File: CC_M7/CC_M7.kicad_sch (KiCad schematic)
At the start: 0 parts

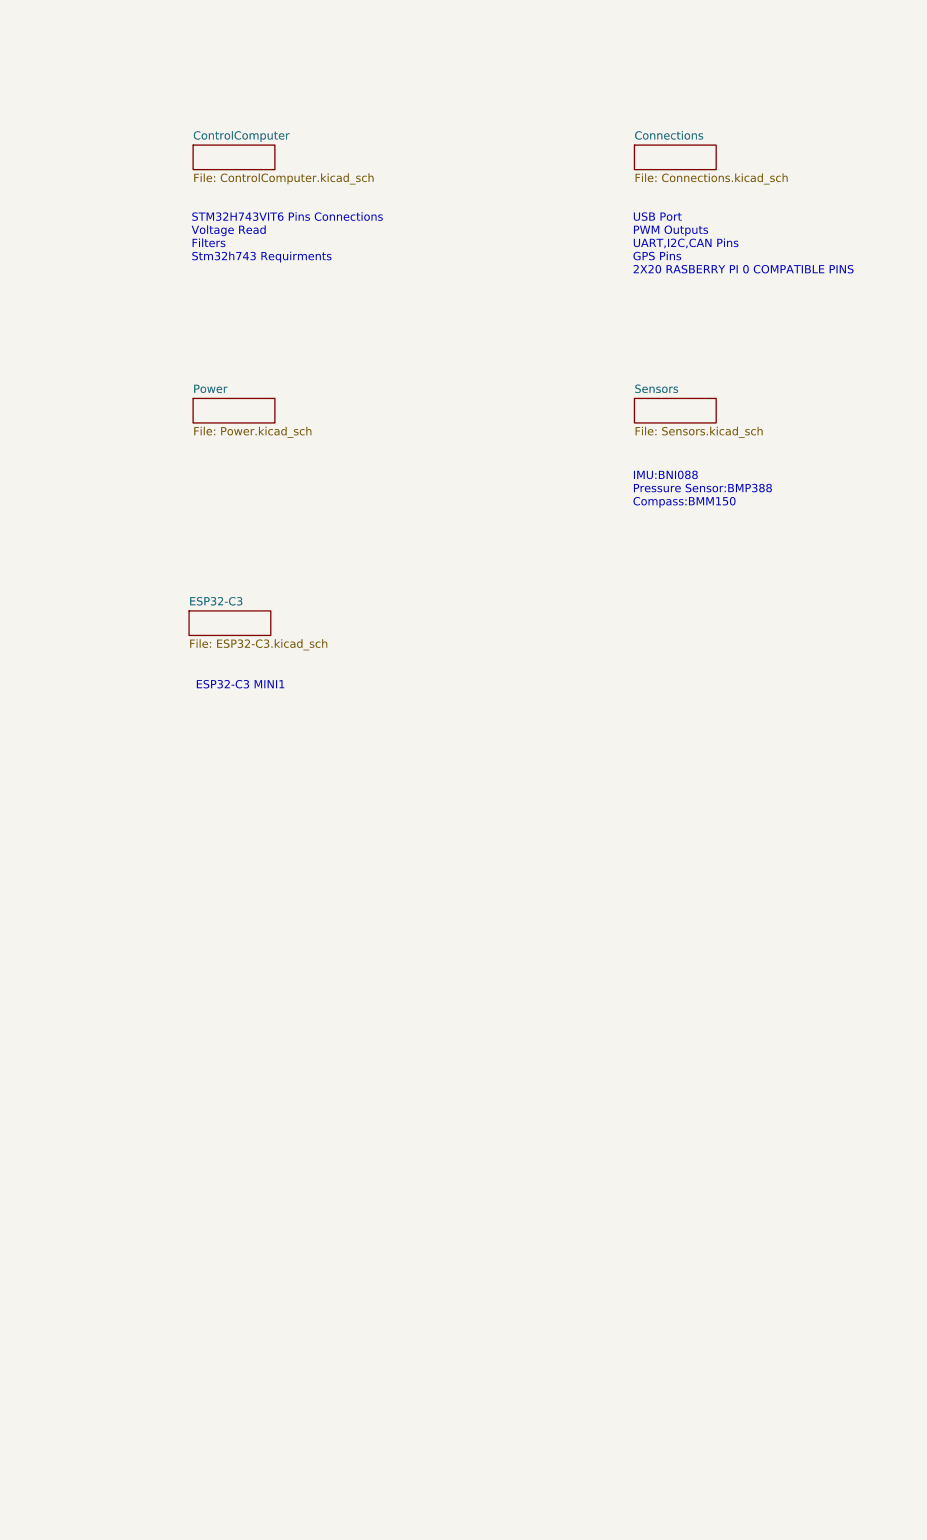
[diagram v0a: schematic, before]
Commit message: update schematic
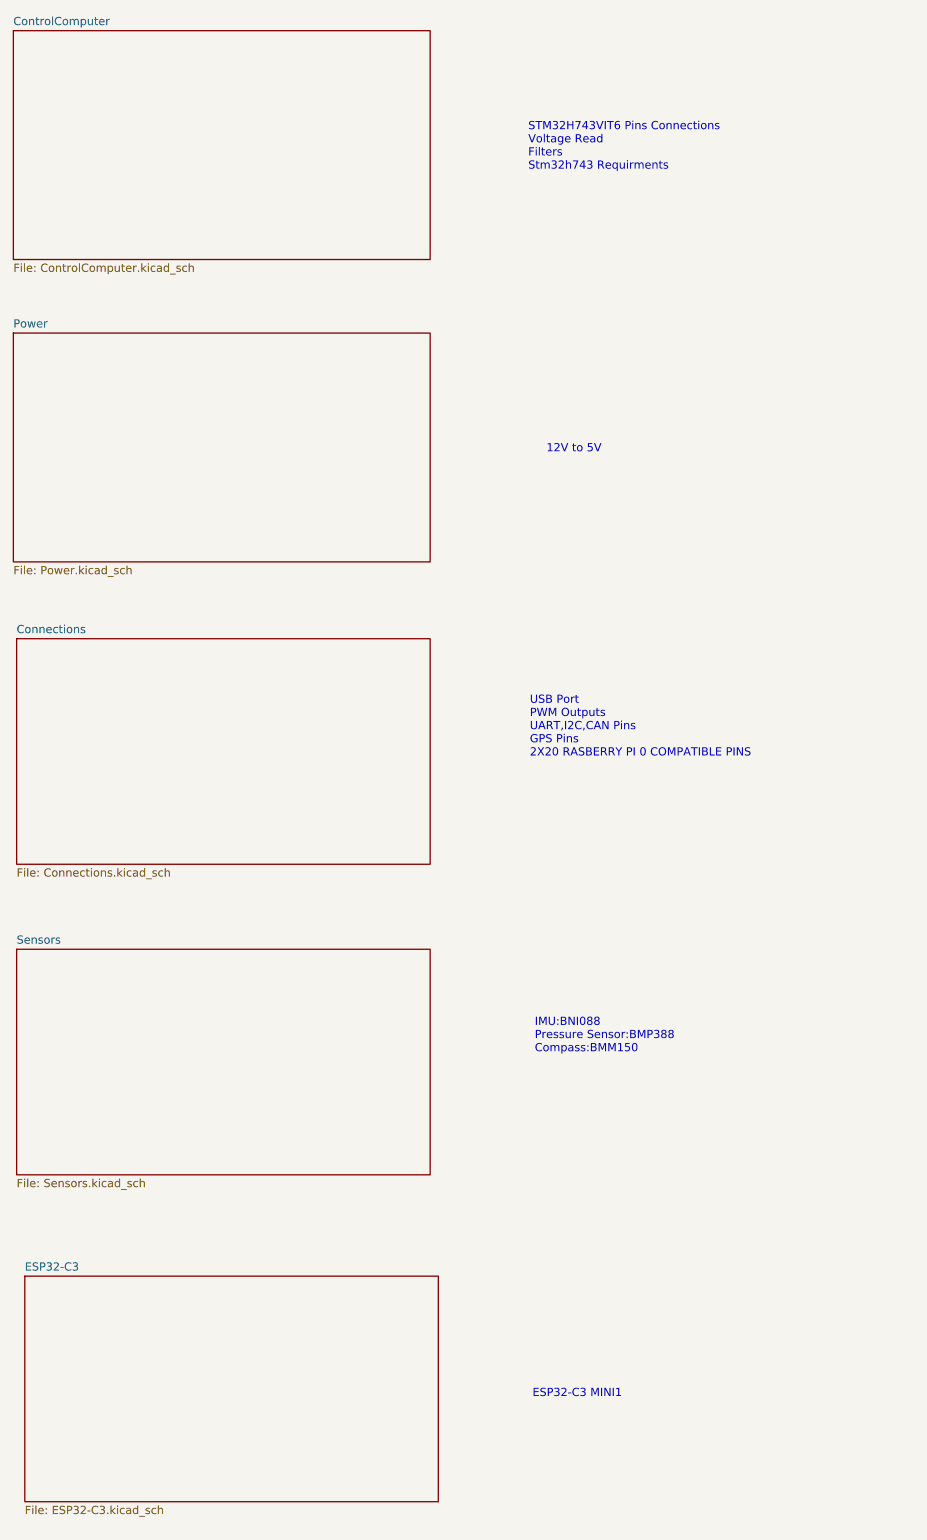
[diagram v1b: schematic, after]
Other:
- note added: "12V to 5V"
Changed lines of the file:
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@@
 		(comment 1 "Stm32 F7 Control Cart")
 	)
+	(text "12V to 5V"
+		(exclude_from_sim no)
+		(at 116.332 85.344 0)
+		(effects
+			(font
+				(size 1.27 1.27)
+			)
+		)
+	)
 	(text "USB Port\nPWM Outputs\nUART,I2C,CAN Pins\nGPS Pins\n2X20 RASBERRY PI 0 COMPATIBLE PINS"
 		(exclude_from_sim no)
-		(at 125.476 53.594 0)
+		(at 109.474 128.524 0)
 		(effects
 			(font
@@
 	(text "ESP32-C3 MINI1"
 		(exclude_from_sim no)
-		(at 64.516 122.174 0)
+		(at 116.84 232.156 0)
 		(effects
 			(font
@@
 	(text "STM32H743VIT6 Pins Connections\nVoltage Read\nFilters\nStm32h743 Requirments"
 		(exclude_from_sim no)
-		(at 56.896 52.578 0)
+		(at 109.22 38.354 0)
 		(effects
 			(font
@@
 	(text "IMU:BNI088\nPressure Sensor:BMP388\nCompass:BMM150\n"
 		(exclude_from_sim no)
-		(at 125.476 91.694 0)
+		(at 110.236 176.53 0)
 		(effects
 			(font
@@
 	)
 	(sheet
-		(at 57.15 38.1)
-		(size 12.7 3.81)
+		(at 29.21 20.32)
+		(size 64.77 35.56)
 		(fields_autoplaced yes)
 		(stroke
@@
 		)
 		(property "Sheetname" "ControlComputer"
-			(at 57.15 37.3884 0)
+			(at 29.21 19.6084 0)
 			(effects
 				(font
@@
 		)
 		(property "Sheetfile" "ControlComputer.kicad_sch"
-			(at 57.15 42.4946 0)
+			(at 29.21 56.4646 0)
 			(effects
 				(font
@@
 	)
 	(sheet
-		(at 56.515 110.49)
-		(size 12.7 3.81)
+		(at 30.988 213.868)
+		(size 64.262 35.052)
 		(fields_autoplaced yes)
 		(stroke
@@
 		)
 		(property "Sheetname" "ESP32-C3"
-			(at 56.515 109.7784 0)
+			(at 30.988 213.1564 0)
 			(effects
 				(font
@@
 		)
 		(property "Sheetfile" "ESP32-C3.kicad_sch"
-			(at 56.515 114.8846 0)
+			(at 30.988 249.5046 0)
 			(effects
 				(font
@@
 	)
 	(sheet
-		(at 125.73 38.1)
-		(size 12.7 3.81)
+		(at 29.718 114.808)
+		(size 64.262 35.052)
 		(fields_autoplaced yes)
 		(stroke
@@
 		)
 		(property "Sheetname" "Connections"
-			(at 125.73 37.3884 0)
+			(at 29.718 114.0964 0)
 			(effects
 				(font
@@
 		)
 		(property "Sheetfile" "Connections.kicad_sch"
-			(at 125.73 42.4946 0)
+			(at 29.718 150.4446 0)
 			(effects
 				(font
@@
 	)
 	(sheet
-		(at 125.73 77.47)
-		(size 12.7 3.81)
+		(at 29.718 163.068)
+		(size 64.262 35.052)
 		(fields_autoplaced yes)
 		(stroke
@@
 		)
 		(property "Sheetname" "Sensors"
-			(at 125.73 76.7584 0)
+			(at 29.718 162.3564 0)
 			(effects
 				(font
@@
 		)
 		(property "Sheetfile" "Sensors.kicad_sch"
-			(at 125.73 81.8646 0)
+			(at 29.718 198.7046 0)
 			(effects
 				(font
@@
 	)
 	(sheet
-		(at 57.15 77.47)
-		(size 12.7 3.81)
+		(at 29.21 67.31)
+		(size 64.77 35.56)
 		(fields_autoplaced yes)
 		(stroke
@@
 		)
 		(property "Sheetname" "Power"
-			(at 57.15 76.7584 0)
+			(at 29.21 66.5984 0)
 			(effects
 				(font
@@
 		)
 		(property "Sheetfile" "Power.kicad_sch"
-			(at 57.15 81.8646 0)
-			(effects
-				(font
+			(at 29.21 103.4546 0)
+			(effects
+				(font

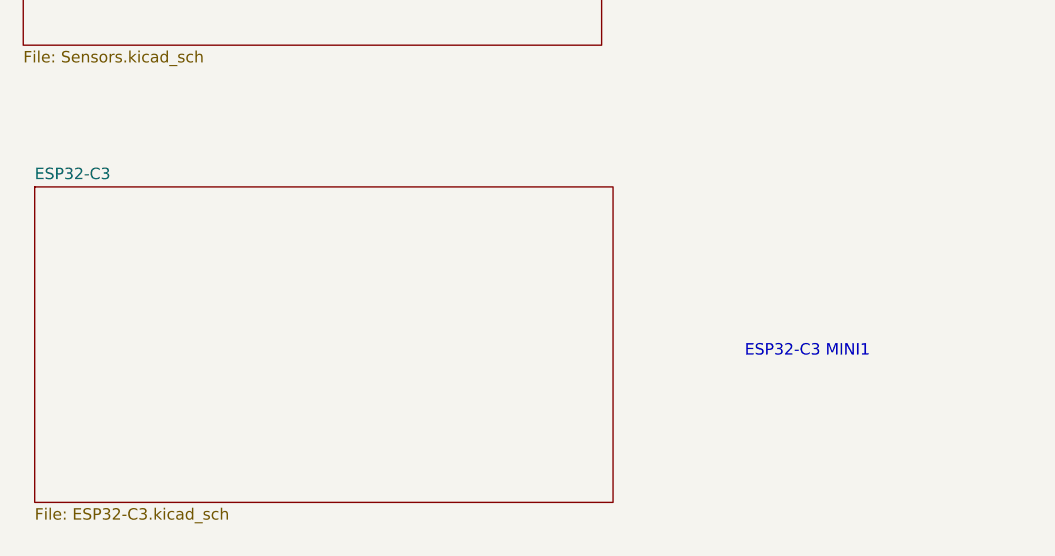
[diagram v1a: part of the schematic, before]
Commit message: nRF52820+nRf21540 add
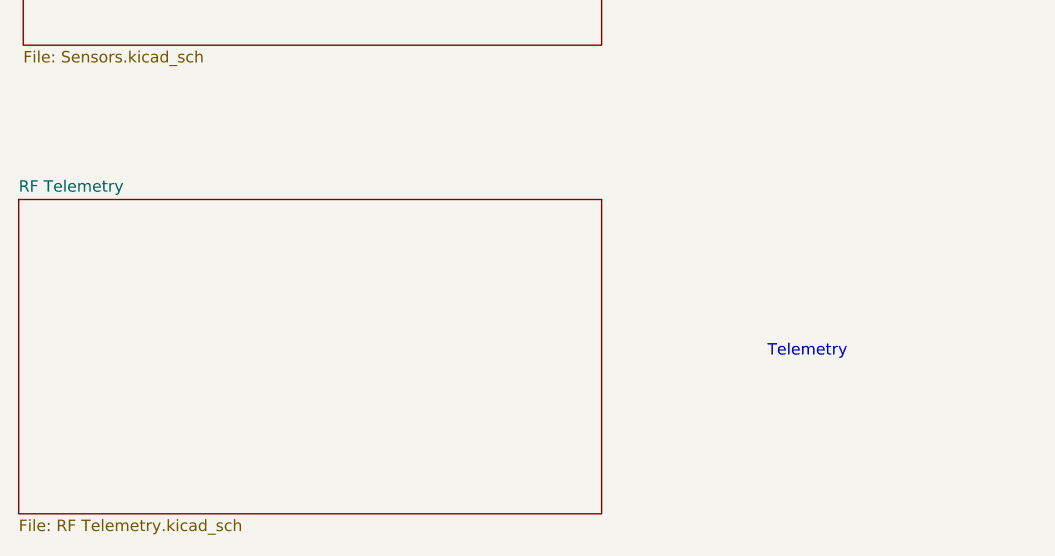
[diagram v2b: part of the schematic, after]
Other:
- removed sheet ESP32-C3
- added sheet RF Telemetry (RF Telemetry.kicad_sch)
- note added: "Telemetry"
- note removed: "ESP32-C3 MINI1"
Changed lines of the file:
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@@
 		)
 	)
-	(text "ESP32-C3 MINI1"
+	(text "Telemetry"
 		(exclude_from_sim no)
 		(at 116.84 232.156 0)
@@
 	)
 	(sheet
-		(at 30.988 213.868)
-		(size 64.262 35.052)
+		(at 29.21 215.265)
+		(size 64.77 34.925)
 		(fields_autoplaced yes)
 		(stroke
@@
 			(color 0 0 0 0.0000)
 		)
-		(property "Sheetname" "ESP32-C3"
-			(at 30.988 213.1564 0)
+		(property "Sheetname" "RF Telemetry"
+			(at 29.21 214.5534 0)
 			(effects
 				(font
@@
 			)
 		)
-		(property "Sheetfile" "ESP32-C3.kicad_sch"
-			(at 30.988 249.5046 0)
+		(property "Sheetfile" "RF Telemetry.kicad_sch"
+			(at 29.21 250.7746 0)
 			(effects
 				(font
